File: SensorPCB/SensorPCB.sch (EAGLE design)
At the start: 27 parts, among them X1 MINI-USB-SCHIELD-32005-201

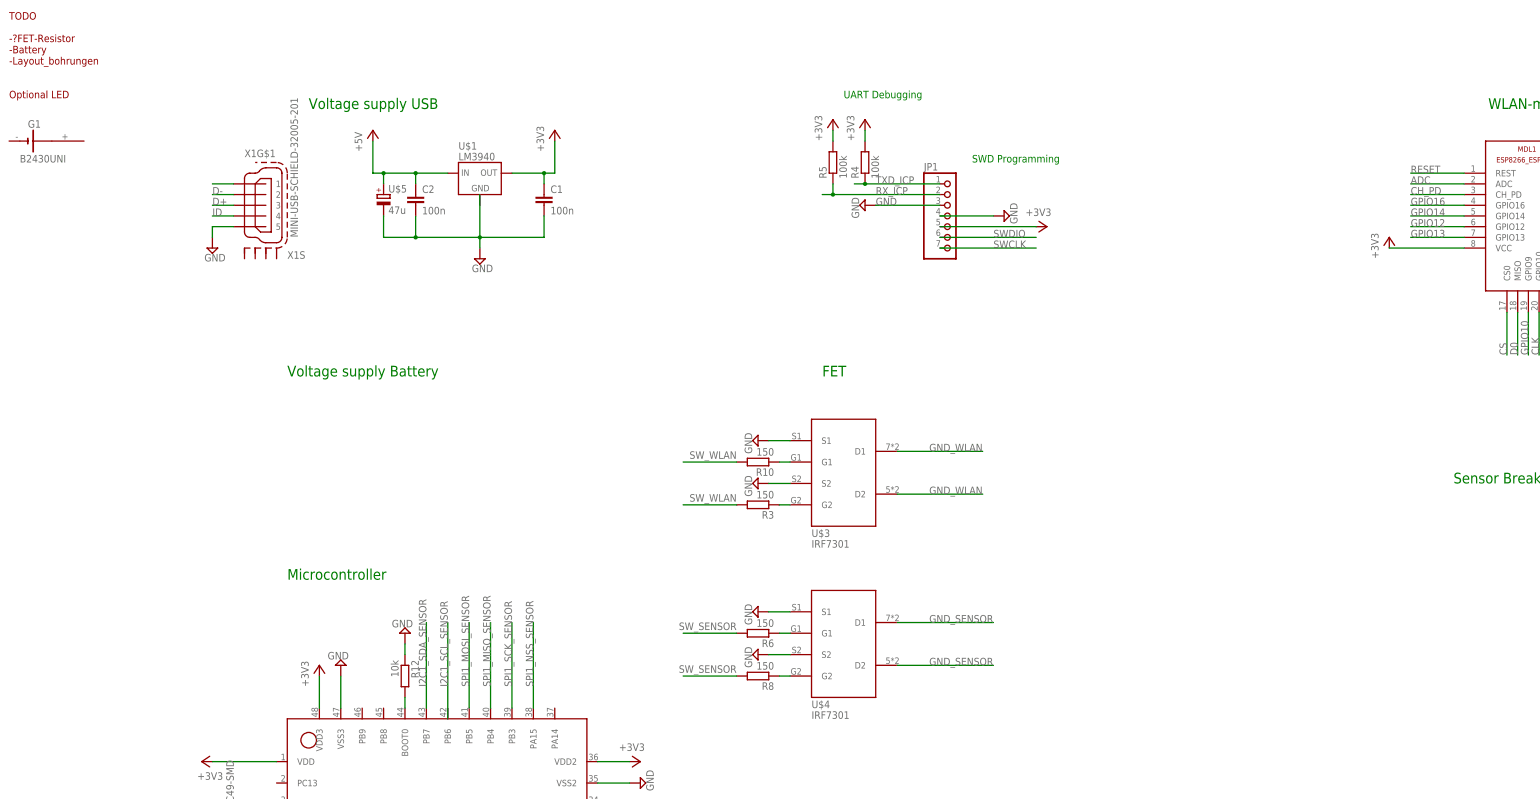
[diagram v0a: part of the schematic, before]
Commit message: add FET pull down resistor
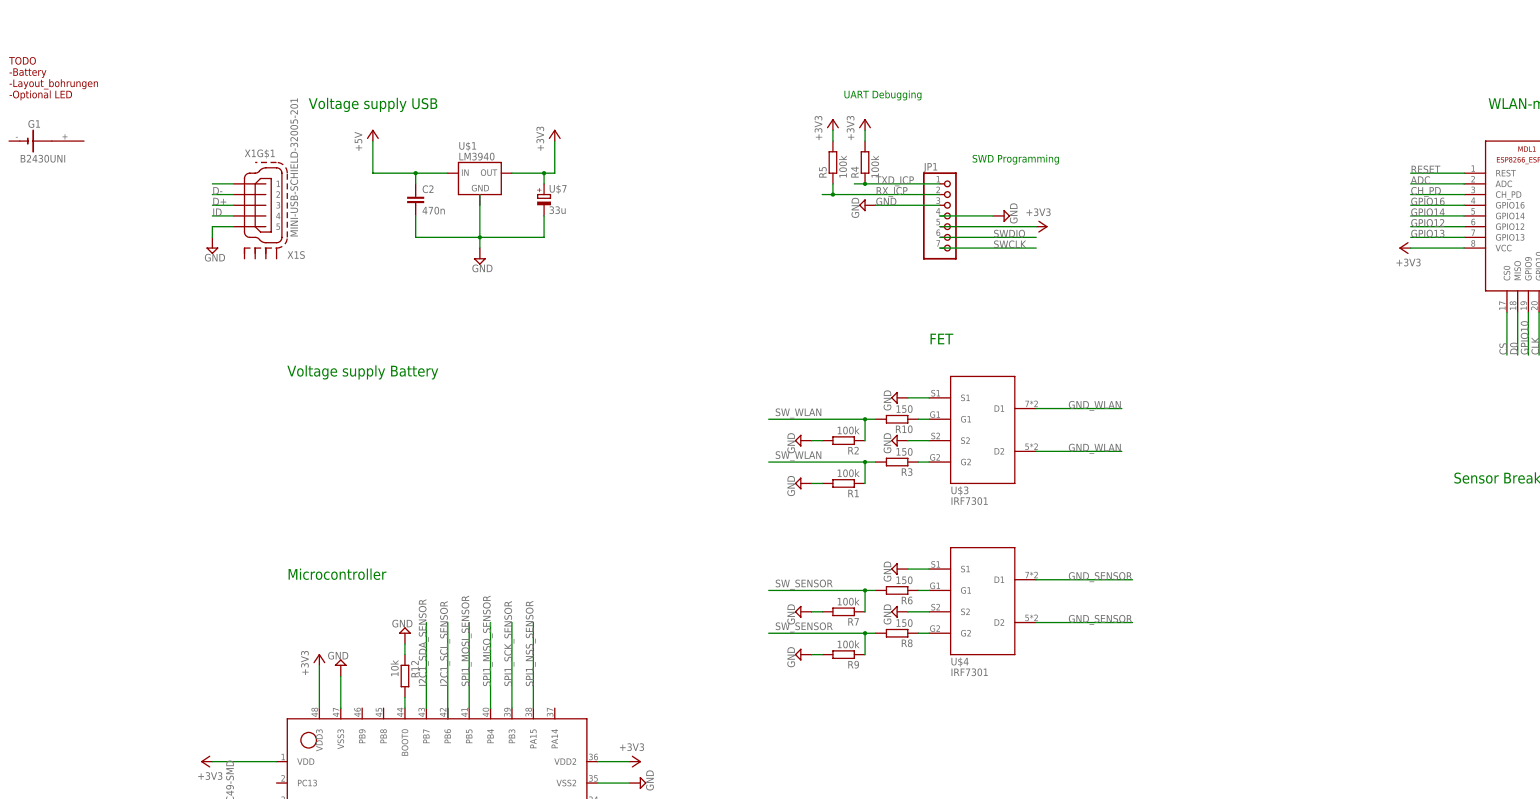
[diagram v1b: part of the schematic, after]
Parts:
- removed C1: 100n, rcl:C-EUC1206
- removed U$5: 47u, CAP_TANTAL_1206:CAP_TANTAL_1206
- added R1, R2, R7, R9: 100k, rcl:R-EU_R1206
- added U$7: 33u, CAP_TANTAL_1206:CAP_TANTAL_1206
- C2: value 100n -> 470n
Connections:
- net +3V3: now also U$7.+; no longer C1.1
- net +5V: no longer U$5.+
- net GND: now also R1.2, R2.2, R7.2, R9.2, U$7.-; no longer C1.2, U$5.-
- net SW_SENSOR: now also R7.1, R9.1
- net SW_WLAN: now also R1.1, R2.1
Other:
- note added: "TODO -Battery -Layout_bohrungen -Optional LED"
- note removed: "TODO -?FET-Resistor -Battery -Layout_bohrungen Optional LED"
- moved on the sheet: R10, R3, R6, R8, U$3, U$4

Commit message: Schematic update
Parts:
- removed R10: 150, rcl:R-EU_R1206
- removed R9: 100k, rcl:R-EU_R1206
- R2: value 100k -> 150
- R6: value 150 -> 100k
- R7: value 100k -> 10k
- R8: value 150 -> 10k
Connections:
- removed net N$2: R10.1, R3.1, U$3.G1, U$3.G2
- new net GATE_SENSOR: R2.1, U$4.G1, U$4.G2
- new net GATE_WLAN: R3.1, U$3.G1, U$3.G2
- new net I2C1_SCL_SENSOR: U$6.PB6
- net ADC: now also R7.1, R8.2, U$6.PA0
- net GND: now also R6.2; no longer R2.2, R9.2
- net N$1: now also U$6.PA1; no longer R6.1, U$4.G1, U$4.G2
- net SW_SENSOR: now also R2.2, R6.1; no longer R6.2, R7.1, R8.2, R9.1
- net SW_WLAN: no longer R10.2, R2.1
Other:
- note added: "check batterie voltage"
- moved on the sheet: C10, C3, C4, C5, C6, C8, C9, R1, R11, R12, R2, R3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

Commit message: fettes update mit Breakout board
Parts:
- added U$5: BREAKOUT_FP_V1, breakout_base:BREAKOUT_FP_V1
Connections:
- new net PA2: U$5.PA2, U$6.PA2
- new net PA3: U$5.PA3, U$6.PA3
- new net PA4: U$5.PA4, U$6.PA4
- new net PA5: U$5.PA5, U$6.PA5
- new net PA6: U$5.PA6, U$6.PA6
- new net PA7: U$5.PA7, U$6.PA7
- new net PB0: U$5.PB0, U$6.PB0
- new net PB1: U$5.PB1, U$6.PB1
- new net PB2: U$5.PB2, U$6.PB2
- net +3V3: now also U$5.3V
- net GND: now also U$5.GND
- net GND_SENSOR: now also U$5.GND_SW
- net I2C1_SCL_SENSOR: now also U$5.PB6/I2C_SCL
- net I2C1_SDA_SENSOR: now also U$5.PB7/I2C_SDA
- net SPI1_MISO_SENSOR: now also U$5.PB4/SPI_MISO
- net SPI1_MOSI_SENSOR: now also U$5.PB5/SPI_MOSI
- net SPI1_NSS_SENSOR: now also U$5.PA15/SPI_NSS
- net SPI1_SCK_SENSOR: now also U$5.PB3/SPI_SCK
- net SWCLK: now also U$6.PA14
- net SWDIO: now also U$6.PA13
- net SW_SENSOR: now also U$6.PA11
- net SW_WLAN: now also U$6.PA12
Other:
- note added: "ACHTUNG: Netz "PA2" beim routen checken, sollte nur vom STM zum breakout gehen. Als ich das benannt hab kam ne Meldung dass es das schon gibt, habs aber nicht gefunden."

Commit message: Schematic update
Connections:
- removed net ADC: MDL1.ADC, R7.1, R8.2, U$6.PA0
- removed net CH_PD: MDL1.CH_PD
- removed net CLK: MDL1.GPIO10
- removed net CS: MDL1.CS0
- removed net D0: MDL1.MISO
- removed net D1: MDL1.MOSI
- removed net RESET: MDL1.REST
- new net ADC_WLAN: MDL1.ADC, R7.1, R8.2, U$6.PA0, U$6.PA9
- new net CH_PD_WLAN: MDL1.CH_PD, U$6.PA10
- new net REST_WLAN: MDL1.REST, U$6.PA8
- net GPIO10: now also MDL1.GPIO10; no longer MDL1.GPIO9
- net GPIO9: now also MDL1.GPIO9; no longer MDL1.SCLK
- net SPI2_MISO_WLAN: now also MDL1.MISO
- net SPI2_MOSI_WLAN: now also MDL1.MOSI
- net SPI2_NSS_WLAN: now also MDL1.CS0
- net SPI2_SCK_WLAN: now also MDL1.SCLK
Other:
- note added: "ADD LPUART (LOW POWER UART) for WLAN AND SENSOR"
- note added: "Default Sensor"
- moved on the sheet: U$5

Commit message: Add default Sensor + Add UART
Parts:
- added R10, R9: 1k8, rcl:R-EU_R1206
- added U$9: MCP9808-E/MS, mcp9808:MCP9808-E/MS
- C5, C8: value 10u -> 100n
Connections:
- net PA2 renamed USART2_TX_SENSOR
- net PA3 renamed USART2_RX_SENSOR
- removed net RX_WLAN: MDL1.RXD
- removed net TX_WLAN: MDL1.TXD
- new net ALERT: U$9.ALERT
- new net USART1_RX_WLAN: MDL1.TXD, U$6.PA10
- new net USART1_TX_WLAN: MDL1.RXD, U$6.PA9
- net +3V3: now also R10.2, R9.2, U$9.VDD
- net ADC_WLAN: no longer U$6.PA9
- net CH_PD_WLAN: no longer U$6.PA10
- net GND: now also U$9.A0, U$9.A1, U$9.A2, U$9.GND
- net I2C1_SCL_SENSOR: now also R10.1, U$9.SCL
- net I2C1_SDA_SENSOR: now also R9.1, U$9.SDA
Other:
- note added: "Default Sensor MCP9808 Microchip Temp. Sensor"
- note added: "I2C address 0011000"
- note added: "TODO -Battery -Layout_bohrungen -Optional LED -change R and C to 0805"
- note removed: "ADD LPUART (LOW POWER UART) for WLAN AND SENSOR"
- note removed: "Default Sensor"
- note removed: "TODO -Battery -Layout_bohrungen -Optional LED"
- moved on the sheet: R1, R2, R3, R6, U$5

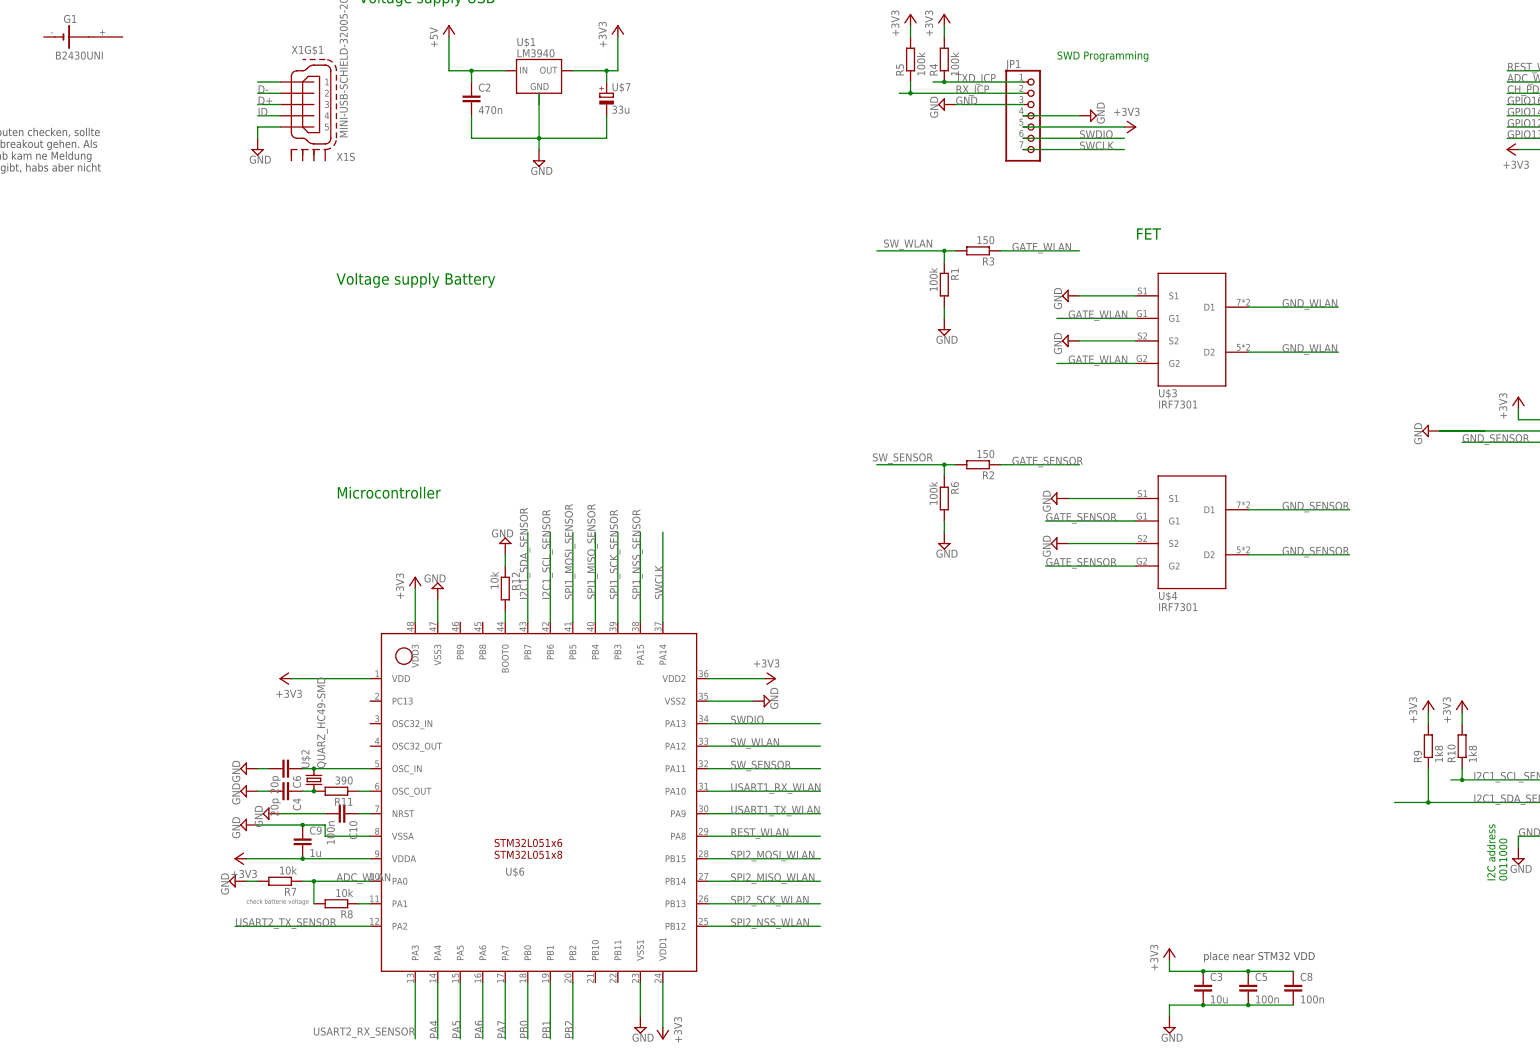
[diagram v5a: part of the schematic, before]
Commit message: change C and R footprint from 1206 to 0805
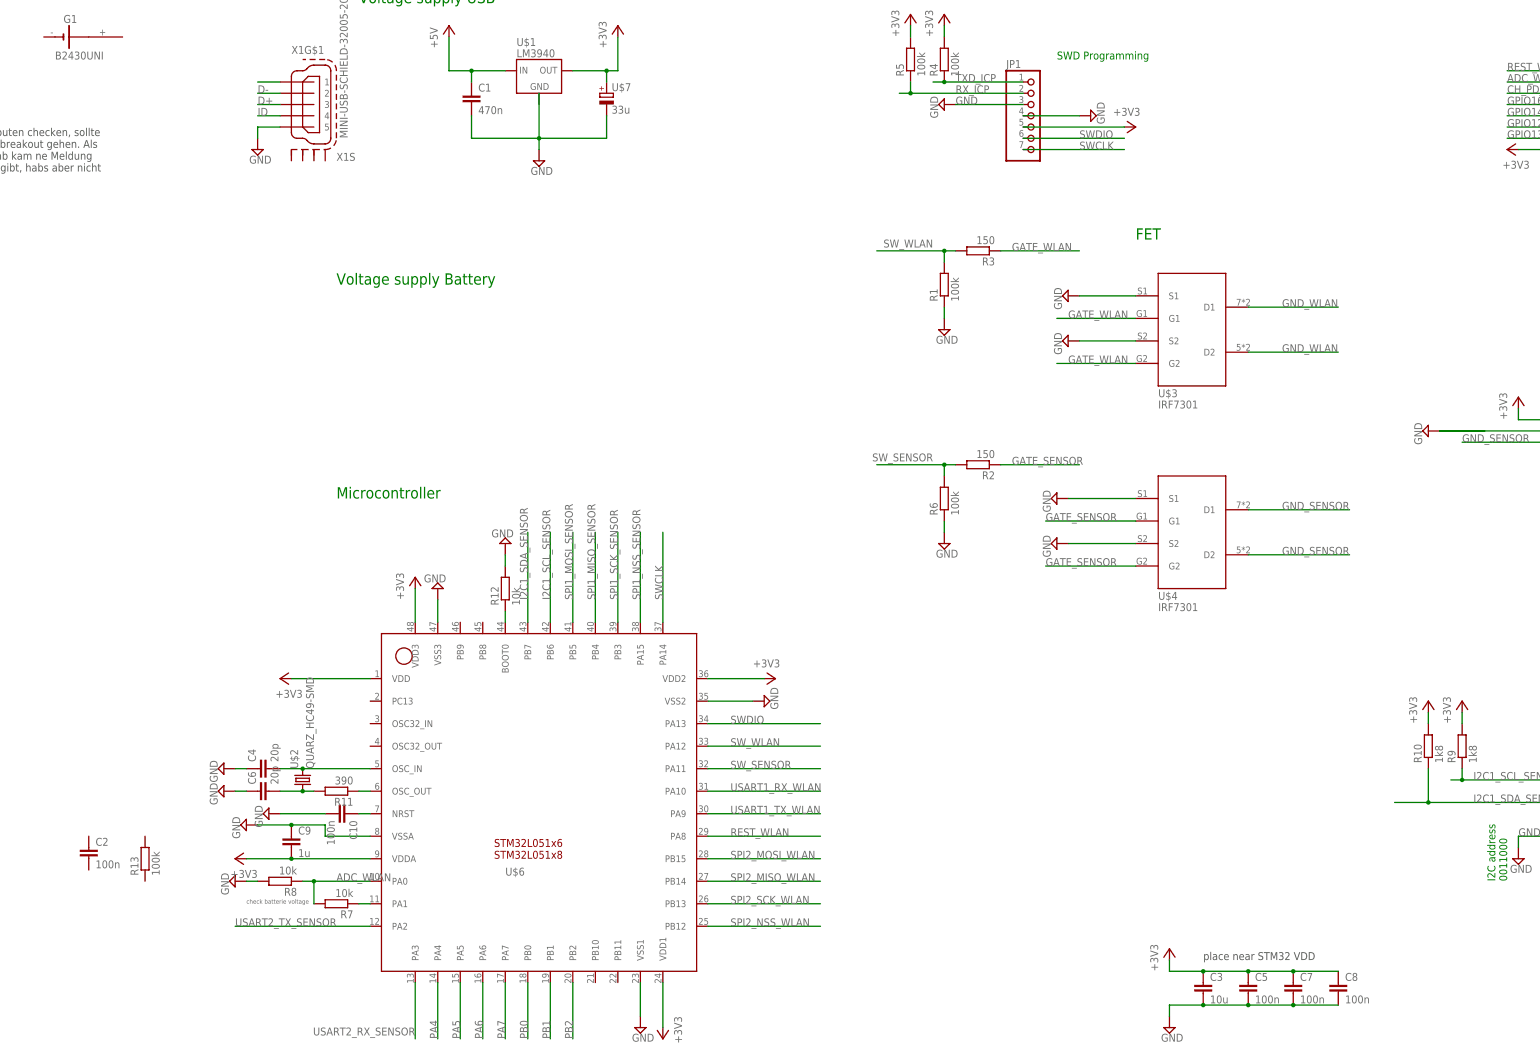
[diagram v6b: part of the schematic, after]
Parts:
- added C1: 470n, rcl:C-EUC0805
- added C7: 100n, rcl:C-EUC0805
- added R13: 100k, rcl:R-EU_R0805
- C10, C3, C4, C5, C6, C8, C9: device rcl:C-EUC1206 -> rcl:C-EUC0805
- C2: value 470n -> 100n; device rcl:C-EUC1206 -> rcl:C-EUC0805
- R1, R10, R11, R12, R2, R3, R4, R5, R6, R7, R8, R9: device rcl:R-EU_R1206 -> rcl:R-EU_R0805
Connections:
- net +3V3: now also C7.1
- net +5V: now also C1.1; no longer C2.1
- net ADC_WLAN: now also R7.2, R8.1; no longer R7.1, R8.2
- net GND: now also C1.2, C4.1, C6.1, C7.2, R1.1, R12.2, R6.1, R8.2; no longer C2.2, C4.2, C6.2, R1.2, R12.1, R6.2, R7.2
- net I2C1_SCL_SENSOR: now also R9.1; no longer R10.1
- net I2C1_SDA_SENSOR: now also R10.1; no longer R9.1
- net N$1: now also R7.1; no longer R8.1
- net N$4: now also C6.2; no longer C4.1
- net N$5: now also C4.2; no longer C6.1
- net N$8: now also R12.1; no longer R12.2
- net SW_SENSOR: now also R6.2; no longer R6.1
- net SW_WLAN: now also R1.2; no longer R1.1
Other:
- moved on the sheet: C2, C4, C6, C8, C9, R1, R10, R12, R6, R7, R8, R9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

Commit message: add first sensor breakout-7board
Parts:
- removed C2: 100n, rcl:C-EUC0805
- removed R13: 100k, rcl:R-EU_R0805
- U$1: WEBSITE (none) -> http://www.reichelt.de/LM-3940-IS3-3/3/index.html?&ACTION=3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
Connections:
- removed net N$3: X1G$1.1
- net +5V: now also X1G$1.1
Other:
- moved on the sheet: C3, C5, C7, C8, R10, R9, U$9

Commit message: change part-name
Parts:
- renumbered JP1 to PHD, MDL1 to ESP8266, U$1 to LM3940, U$2 to QUARZ-HC49, U$3 to IRF7301_WLAN, U$4 to IRF7301_SENSOR, U$6 to STM32L051C8T6, U$9 to MCP9808, X1 to MINI_USB
